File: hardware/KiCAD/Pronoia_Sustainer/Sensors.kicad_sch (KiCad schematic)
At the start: 8 parts, among them U4 ISM330DHCX, U5 MS5611-01BA, U6 H3LIS331DL

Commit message: Last commit for KiCAD schematic w/ GPS, Telem, and Bluetooth
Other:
- company: (none) -> Walla Walla University
- title: (none) -> Pronoia Sustainer Sensors
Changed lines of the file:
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@@
 	(generator_version "9.0")
 	(paper "A4")
+	(title_block
+		(title "Pronoia Sustainer Sensors")
+		(date "2026-02-03")
+		(rev "1.0")
+		(company "Walla Walla University")
+		(comment 1 "Prometheus Rocket Project")
+	)
 	(text "Barometer"
 		(exclude_from_sim no)

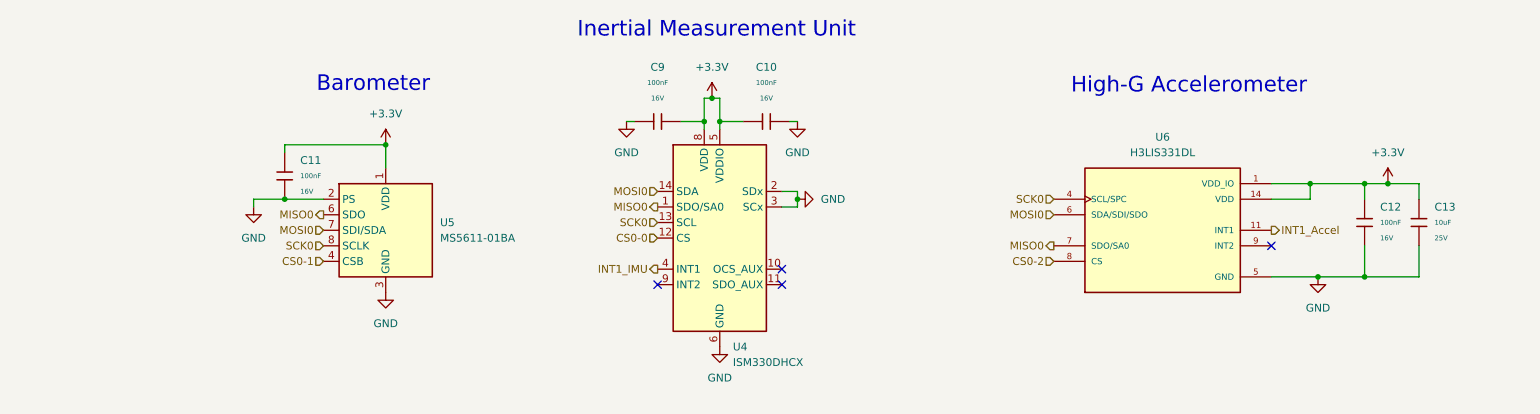
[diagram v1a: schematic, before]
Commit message: Red LED and UI Buzzer Circuit
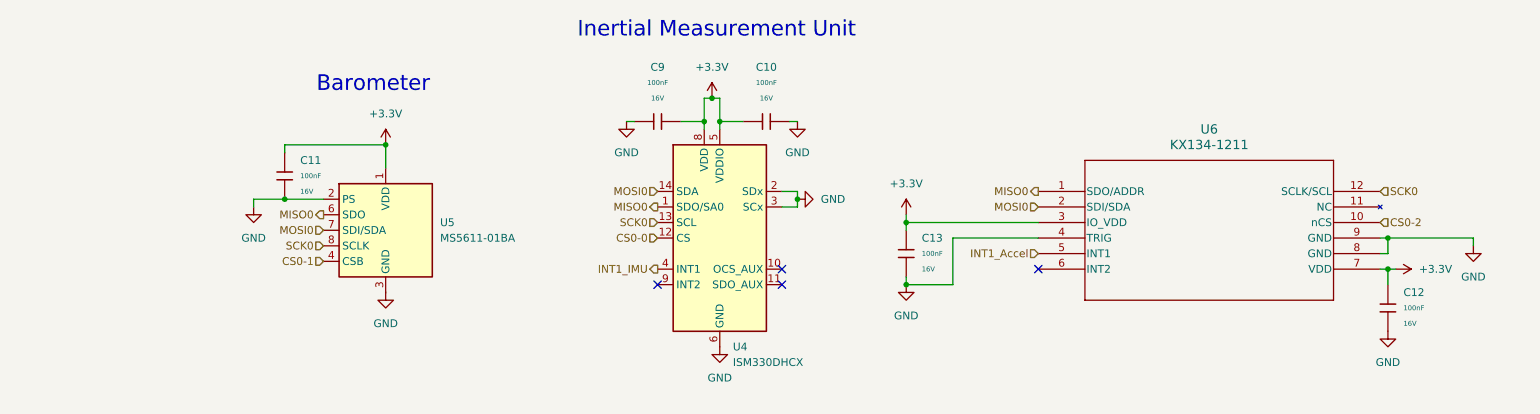
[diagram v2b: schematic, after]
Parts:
- removed C13: 10uF, PCM_JLCPCB:C_0805, symbol PCM_JLCPCB-Capacitors:0805,10uF
- removed U6: H3LIS331DL, H3LIS331DL:QFN300X300X100-16N, symbol H3LIS331DL:H3LIS331DL
- added C13: 100nF, PCM_JLCPCB:C_0402, symbol PCM_JLCPCB-Capacitors:0402,100nF
- added U6: KX134-1211, KX134-1211:KIONIX_KXTJ3-1057, symbol KX134-1211:KX134-1211
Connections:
- net +3.3V: now also C13.2, U6.3 (IO_VDD), U6.7 (VDD)
- net CS0-2: now also U6.10 (nCS)
- net GND: now also C13.1, U6.4 (TRIG), U6.8 (GND), U6.9 (GND)
- net INT1_Accel: now also U6.5 (INT1)
- net MISO0: now also U6.1 (SDO/ADDR)
- net MOSI0: now also U6.2 (SDI/SDA)
- net SCK0: now also U6.12 (SCLK/SCL)
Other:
- note removed: "High-G Accelerometer"

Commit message: Finalized v2.0 of Pronoia Schematic
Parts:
- added R19, R29: 10kΩ, PCM_JLCPCB:R_0805, symbol PCM_JLCPCB-Resistors:0805,10kΩ
- added R30, R31, R32: 33Ω, PCM_JLCPCB:R_0805, symbol PCM_JLCPCB-Resistors:0805,33Ω
- U6: LCSC (none) -> C2157908
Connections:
- net CS0-2 is gone; now on net CS0-1: U6.10 (nCS)
- net CS0-1: no longer U5.4 (CSB), U5.5 (CSB)
- net GND: now also R19.2, R29.2; no longer U4.2 (SDx), U4.3 (SCx)
- net MISO0: now also R30.1, R31.1; no longer U4.1 (SDO/SA0), U5.6 (SDO), U6.1 (SDO/ADDR)
- net MOSI0: no longer U5.7 (SDI/SDA)
- net SCK0: no longer U5.8 (SCLK)
- new net: R19.1, U4.3 (SCx)
- new net: R30.2, U6.1 (SDO/ADDR)
- new net: R31.2, U4.1 (SDO/SA0)
- new net: R29.1, U4.2 (SDx)
- new net: R32.2, U5.6 (SDO)
- new net CS1-0: U5.4 (CSB), U5.5 (CSB)
- new net MISO1: R32.1
- new net MOSI1: U5.7 (SDI/SDA)
- new net SCK1: U5.8 (SCLK)
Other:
- note added: "High-G Accelerometer"
- moved on the sheet: C10, C11, C12, C13, C9, U4, U5, U6

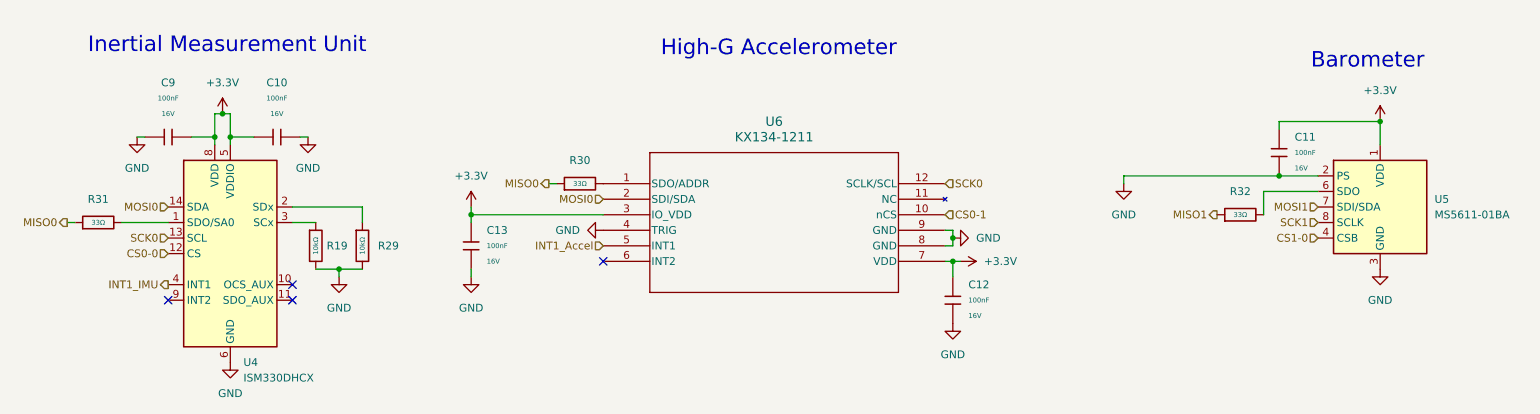
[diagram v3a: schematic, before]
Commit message: Finished PCB layout
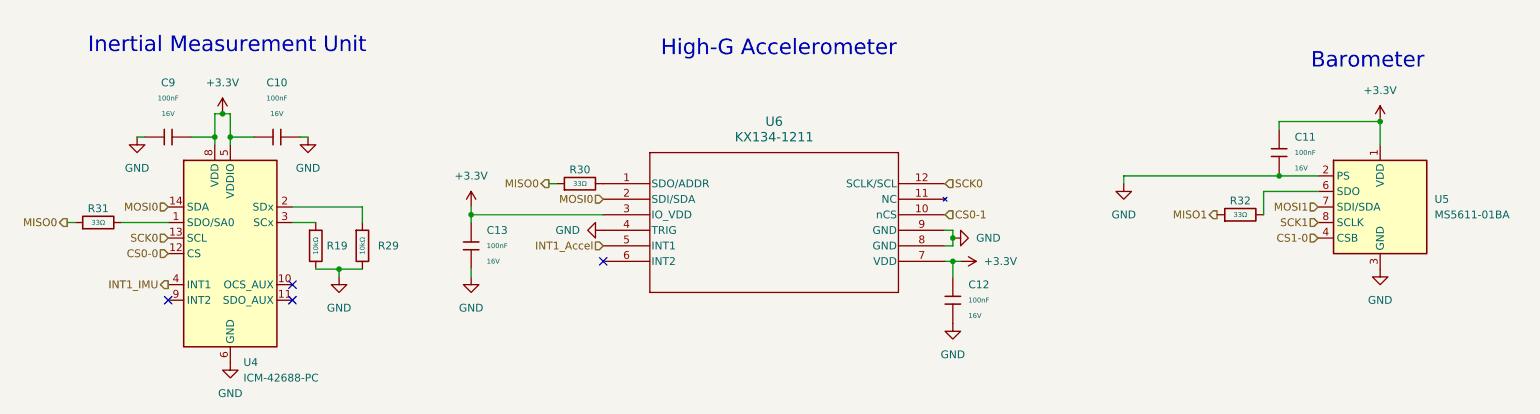
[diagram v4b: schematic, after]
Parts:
- removed R30, R31, R32: 33Ω, PCM_JLCPCB:R_0805, symbol PCM_JLCPCB-Resistors:0805,33Ω
- added R30, R31, R32: 33Ω, PCM_JLCPCB:R_0402, symbol PCM_JLCPCB-Resistors:0402,33Ω
- U4: value ISM330DHCX -> ICM-42688-PC; LCSC C48586482 -> C48586483
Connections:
- net MISO0: now also R30.1, R31.1
- net MISO1: now also R32.1
- net at U6.1 (SDO/ADDR): now also R30.2
- net at U4.1 (SDO/SA0): now also R31.2
- net at U5.6 (SDO): now also R32.2
